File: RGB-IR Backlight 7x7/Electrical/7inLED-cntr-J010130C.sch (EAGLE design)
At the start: 52 parts, among them M1 TEENSY_3.1-3.2_DIL, P3 CON2X3, U1 LP2985-33DBVR, U2 AD5624R-3, U24 IL 710, U3 OPA4197IDR, U4 OPA4197IDR, U5 LMV344, U6 LMV344, U8 741G3157DBVR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

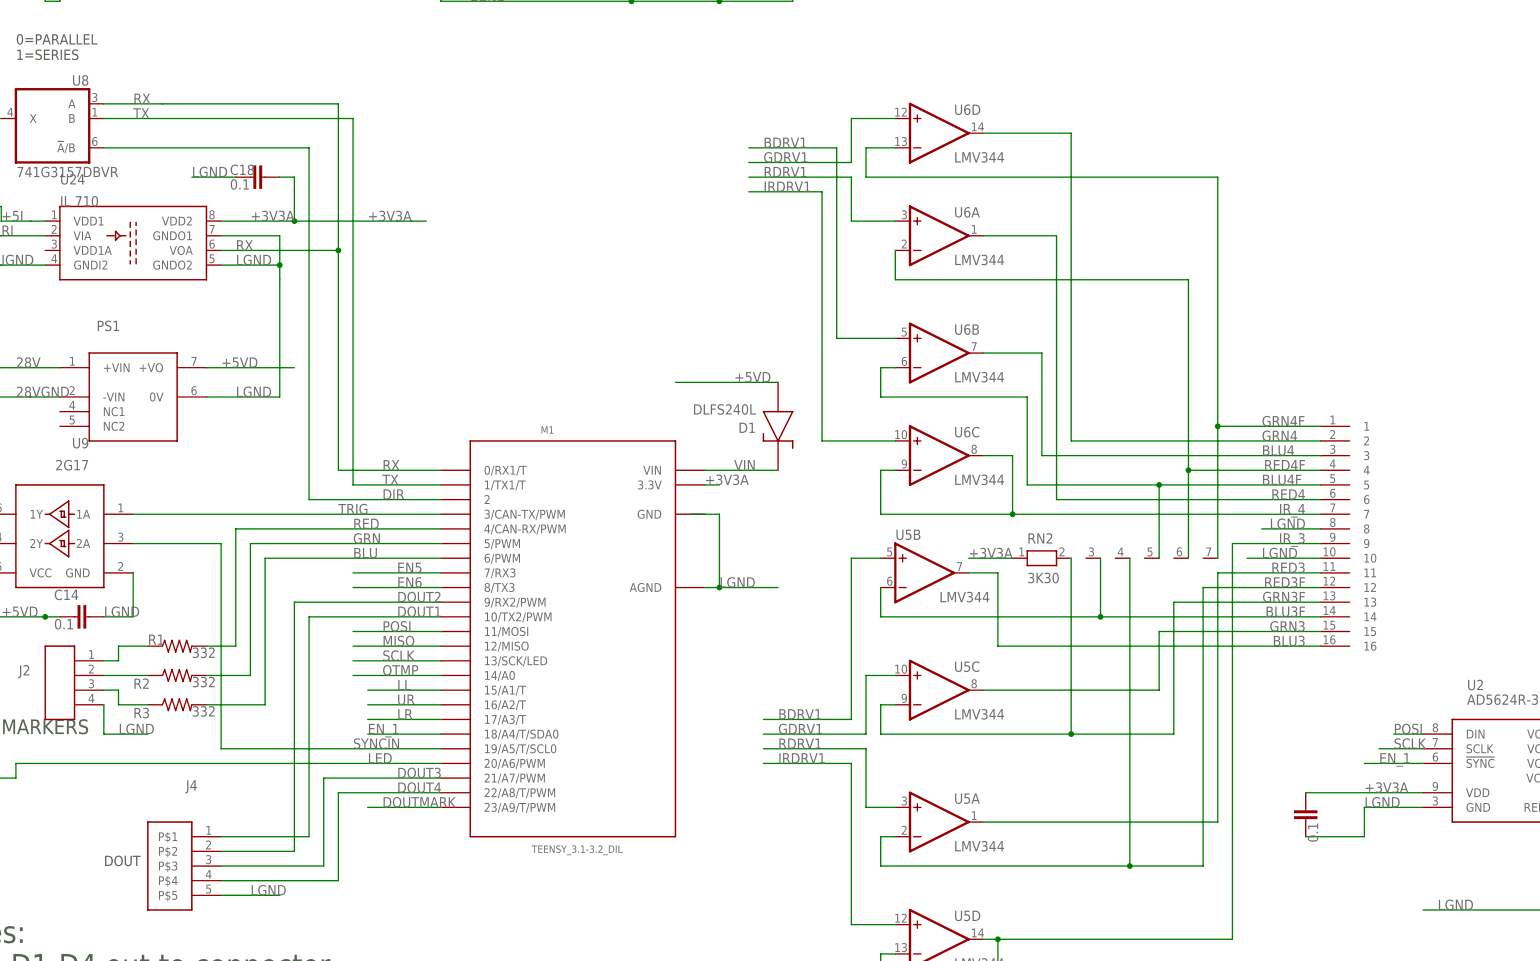
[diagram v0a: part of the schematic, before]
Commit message: board change and FW update
Change Teensy connector to two parts so it can be put into Circuithub
Fix markerCmd - digital changes weren't changing pin state
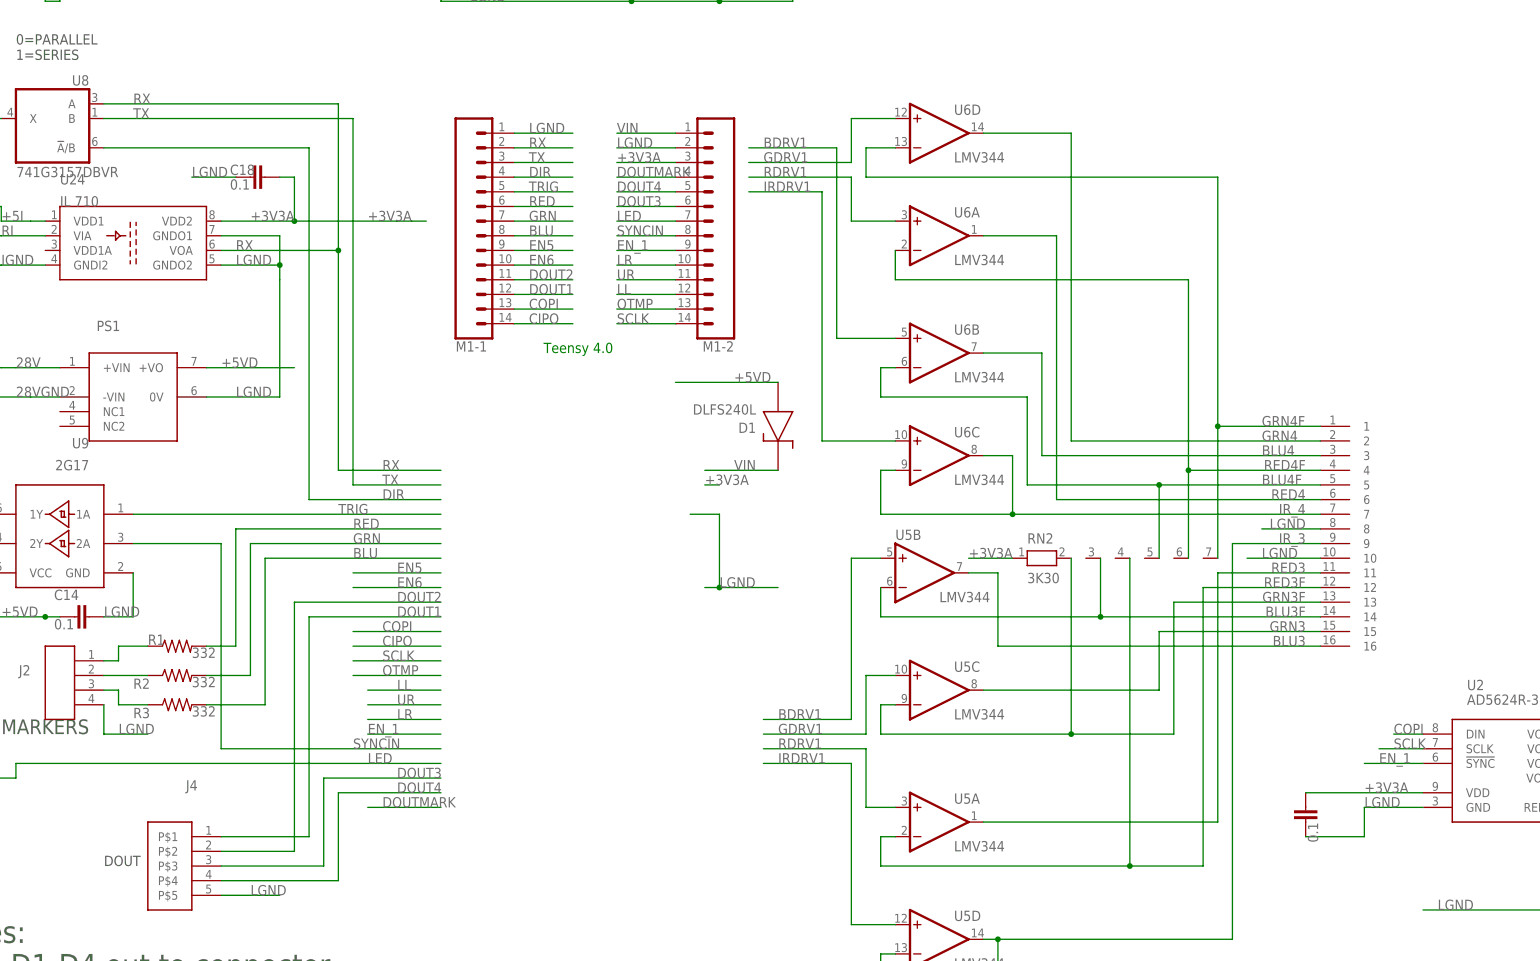
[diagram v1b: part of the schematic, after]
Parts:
- removed M1: TEENSY_3.1-3.2_DIL, Teensy_3_and_LC_Series_Boards_v1.4:TEENSY_3.1-3.2_DIL
- added M1-1, M1-2: (no value), SparkFun-Connectors:CONN_14
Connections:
- removed net MISO: M1.12/MISO
- removed net POSI: M1.11/MOSI, U2.DIN
- new net CIPO: M1-1.14
- new net COPI: M1-1.13, U2.DIN
- net +3V3A: now also M1-2.3; no longer M1.3.3V
- net BLU: now also M1-1.8; no longer M1.6/PWM
- net DIR: now also M1-1.4; no longer M1.2
- net DOUT1: now also M1-1.12; no longer M1.10/TX2/PWM
- net DOUT2: now also M1-1.11; no longer M1.9/RX2/PWM
- net DOUT3: now also M1-2.6; no longer M1.21/A7/PWM
- net DOUT4: now also M1-2.5; no longer M1.22/A8/T/PWM
- net DOUTMARK: now also M1-2.4; no longer M1.23/A9/T/PWM
- net EN5: now also M1-1.9; no longer M1.7/RX3
- net EN6: now also M1-1.10; no longer M1.8/TX3
- net EN_1: now also M1-2.9; no longer M1.18/A4/T/SDA0
- net GRN: now also M1-1.7; no longer M1.5/PWM
- net LED: now also M1-2.7; no longer M1.20/A6/PWM
- net LGND: now also M1-1.1, M1-2.2; no longer M1.AGND, M1.GND
- net LL: now also M1-2.12; no longer M1.15/A1/T
- net LR: now also M1-2.10; no longer M1.17/A3/T
- net OTMP: now also M1-2.13; no longer M1.14/A0
- net RED: now also M1-1.6; no longer M1.4/CAN-RX/PWM
- net RX: now also M1-1.2; no longer M1.0/RX1/T
- net SCLK: now also M1-2.14; no longer M1.13/SCK/LED
- net SYNCIN: now also M1-2.8; no longer M1.19/A5/T/SCL0
- net TRIG: now also M1-1.5; no longer M1.3/CAN-TX/PWM
- net TX: now also M1-1.3; no longer M1.1/TX1/T
- net UR: now also M1-2.11; no longer M1.16/A2/T
- net VIN: now also M1-2.1; no longer M1.VIN
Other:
- note added: "Teensy 4.0"

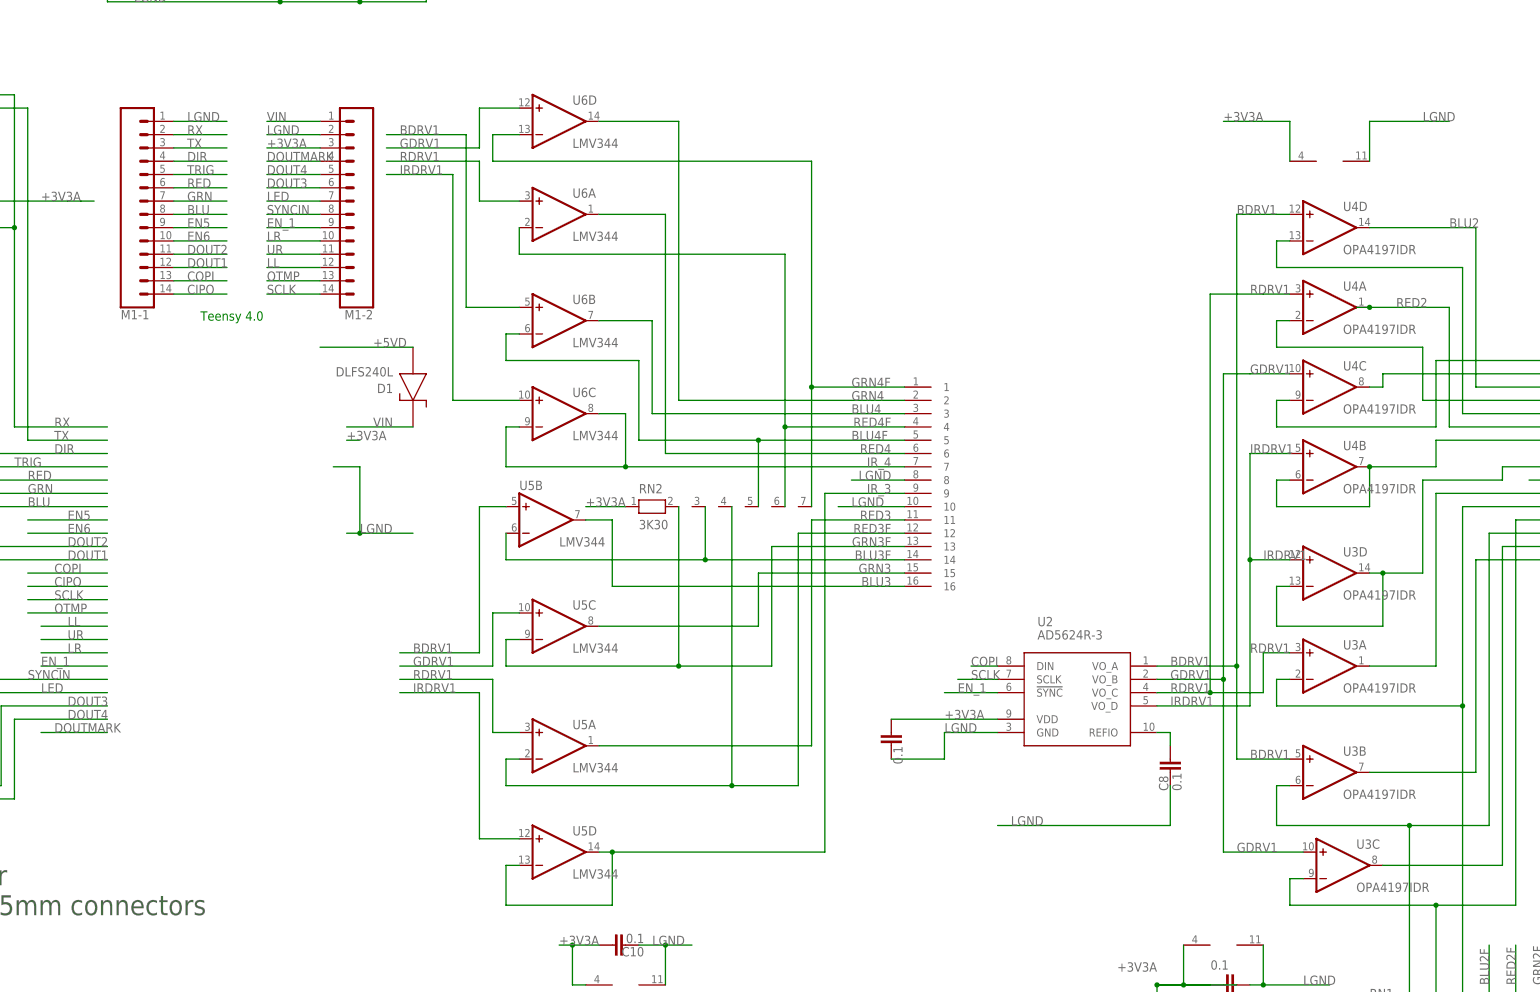
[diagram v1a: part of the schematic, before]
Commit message: Update BOM and firmware
Comment out DEBUG define in FW
Update costing in BOM
Correct quantities, etc in BOM
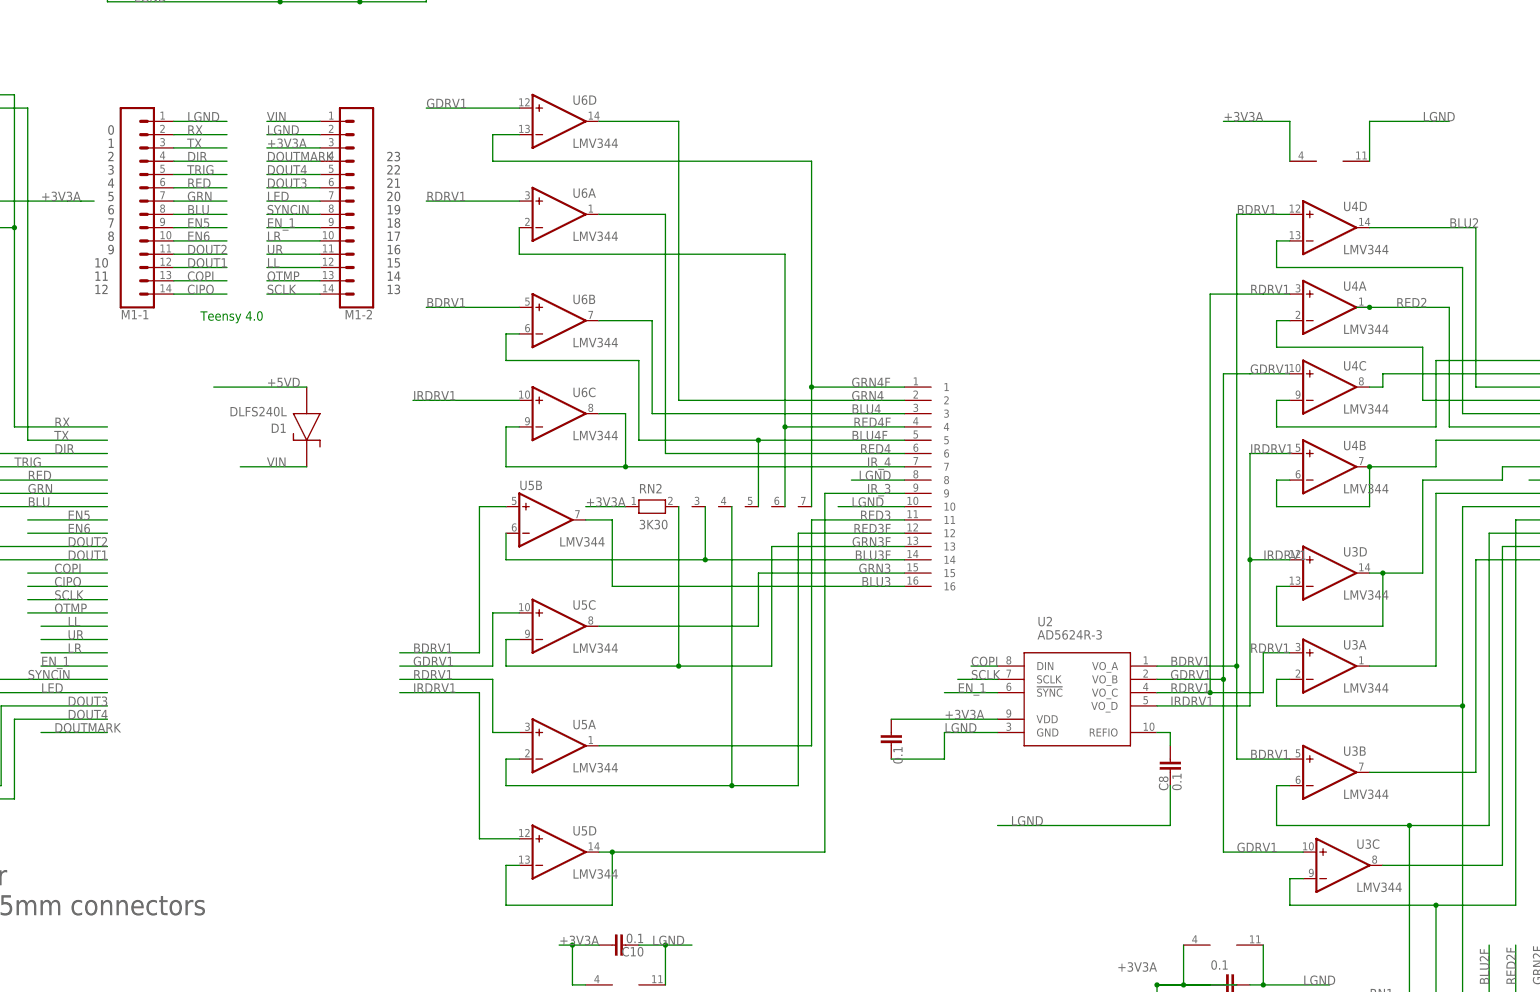
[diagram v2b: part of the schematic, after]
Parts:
- U3, U4: value OPA4197IDR -> LMV344
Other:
- note added: "0"
- note added: "1"
- note added: "10"
- note added: "11"
- note added: "12"
- note added: "13"
- note added: "14"
- note added: "15"
- note added: "16"
- note added: "17"
- note added: "18"
- note added: "19"
- note added: "2"
- note added: "20"
- note added: "21"
- note added: "22"
- note added: "23"
- note added: "3"
- note added: "4"
- note added: "5"
- note added: "6"
- note added: "7"
- note added: "8"
- note added: "9"
- moved on the sheet: D1
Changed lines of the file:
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@@
 <part name="C8" library="STEVES_BU" deviceset="CAPS" device="0603S" value="0.1"/>
 <part name="P1" library="STEVES_BU" deviceset="CON16" device="2X8PLUG"/>
-<part name="U4" library="adafruit" deviceset="QUAD_OPAMP" device="D" value="OPA4197IDR"/>
-<part name="U3" library="adafruit" deviceset="QUAD_OPAMP" device="D" value="OPA4197IDR"/>
+<part name="U4" library="adafruit" deviceset="QUAD_OPAMP" device="D" value="LMV344"/>
+<part name="U3" library="adafruit" deviceset="QUAD_OPAMP" device="D" value="LMV344"/>
 <part name="U5" library="adafruit" deviceset="QUAD_OPAMP" device="D" value="LMV344"/>
 <part name="U6" library="adafruit" deviceset="QUAD_OPAMP" device="D" value="LMV344"/>
@@
 <text x="281.94" y="177.8" size="1.778" layer="97">DOUT</text>
 <text x="358.14" y="266.7" size="1.778" layer="91">Teensy 4.0</text>
+<text x="340.36" y="302.26" size="1.778" layer="97">0</text>
+<text x="340.36" y="299.72" size="1.778" layer="97">1</text>
+<text x="340.36" y="297.18" size="1.778" layer="97">2</text>
+<text x="340.36" y="294.64" size="1.778" layer="97">3</text>
+<text x="340.36" y="292.1" size="1.778" layer="97">4</text>
+<text x="340.36" y="289.56" size="1.778" layer="97">5</text>
+<text x="340.36" y="287.02" size="1.778" layer="97">6</text>
+<text x="340.36" y="284.48" size="1.778" layer="97">7</text>
+<text x="340.36" y="281.94" size="1.778" layer="97">8</text>
+<text x="340.36" y="279.4" size="1.778" layer="97">9</text>
+<text x="337.82" y="276.86" size="1.778" layer="97">10</text>
+<text x="337.82" y="274.32" size="1.778" layer="97">11</text>
+<text x="337.82" y="271.78" size="1.778" layer="97">12</text>
+<text x="393.7" y="271.78" size="1.778" layer="97">13</text>
+<text x="393.7" y="274.32" size="1.778" layer="97">14</text>
+<text x="393.7" y="276.86" size="1.778" layer="97">15</text>
+<text x="393.7" y="279.4" size="1.778" layer="97">16</text>
+<text x="393.7" y="281.94" size="1.778" layer="97">17</text>
+<text x="393.7" y="284.48" size="1.778" layer="97">18</text>
+<text x="393.7" y="287.02" size="1.778" layer="97">19</text>
+<text x="393.7" y="289.56" size="1.778" layer="97">20</text>
+<text x="393.7" y="292.1" size="1.778" layer="97">21</text>
+<text x="393.7" y="294.64" size="1.778" layer="97">22</text>
+<text x="393.7" y="297.18" size="1.778" layer="97">23</text>
 </plain>
 <instances>
@@
 <attribute name="VALUE" x="303.784" y="295.021" size="1.778" layer="96"/>
 </instance>
-<instance part="D1" gate="G$1" x="398.78" y="254" smashed="yes" rot="R270">
-<attribute name="NAME" x="394.97" y="254.635" size="1.778" layer="95" rot="R180"/>
-<attribute name="VALUE" x="394.97" y="257.81" size="1.778" layer="96" rot="R180"/>
+<instance part="D1" gate="G$1" x="378.46" y="246.38" smashed="yes" rot="R270">
+<attribute name="NAME" x="374.65" y="247.015" size="1.778" layer="95" rot="R180"/>
+<attribute name="VALUE" x="374.65" y="250.19" size="1.778" layer="96" rot="R180"/>
 </instance>
 <instance part="J3" gate="G$1" x="228.6" y="238.76" rot="MR0"/>
@@
 <wire x1="492.76" y1="236.22" x2="482.6" y2="236.22" width="0.1524" layer="91"/>
 <label x="490.22" y="236.22" size="1.778" layer="95" rot="MR0"/>
-</segment>
-<segment>
-<wire x1="383.54" y1="238.76" x2="388.62" y2="238.76" width="0.1524" layer="91"/>
-<wire x1="388.62" y1="238.76" x2="388.62" y2="226.06" width="0.1524" layer="91"/>
-<wire x1="388.62" y1="226.06" x2="386.08" y2="226.06" width="0.1524" layer="91"/>
-<label x="388.62" y="226.06" size="1.778" layer="95"/>
-<wire x1="388.62" y1="226.06" x2="398.78" y2="226.06" width="0.1524" layer="91"/>
-<junction x="388.62" y="226.06"/>
 </segment>
 <segment>
@@
 <segment>
 <pinref part="D1" gate="G$1" pin="A"/>
-<wire x1="398.78" y1="261.62" x2="381" y2="261.62" width="0.1524" layer="91"/>
-<label x="391.16" y="261.62" size="1.778" layer="95"/>
+<wire x1="378.46" y1="254" x2="360.68" y2="254" width="0.1524" layer="91"/>
+<label x="370.84" y="254" size="1.778" layer="95"/>
 </segment>
 <segment>
@@
 </segment>
 <segment>
-<label x="396.24" y="302.26" size="1.778" layer="95"/>
+<label x="401.32" y="269.24" size="1.778" layer="95"/>
 <pinref part="U6" gate="B" pin="+IN"/>
-<wire x1="419.1" y1="269.24" x2="408.94" y2="269.24" width="0.1524" layer="91"/>
-<wire x1="408.94" y1="269.24" x2="408.94" y2="302.26" width="0.1524" layer="91"/>
-<wire x1="408.94" y1="302.26" x2="393.7" y2="302.26" width="0.1524" layer="91"/>
+<wire x1="419.1" y1="269.24" x2="401.32" y2="269.24" width="0.1524" layer="91"/>
 </segment>
 <segment>
@@
 </segment>
 <segment>
-<label x="396.24" y="299.72" size="1.778" layer="95"/>
-<wire x1="393.7" y1="299.72" x2="411.48" y2="299.72" width="0.1524" layer="91"/>
-<wire x1="411.48" y1="299.72" x2="411.48" y2="307.34" width="0.1524" layer="91"/>
-<wire x1="411.48" y1="307.34" x2="419.1" y2="307.34" width="0.1524" layer="91"/>
+<label x="401.32" y="307.34" size="1.778" layer="95"/>
+<wire x1="401.32" y1="307.34" x2="419.1" y2="307.34" width="0.1524" layer="91"/>
 <pinref part="U6" gate="D" pin="+IN"/>
 </segment>
@@
 </segment>
 <segment>
-<label x="396.24" y="297.18" size="1.778" layer="95"/>
+<label x="401.32" y="289.56" size="1.778" layer="95"/>
 <pinref part="U6" gate="A" pin="+IN"/>
-<wire x1="419.1" y1="289.56" x2="411.48" y2="289.56" width="0.1524" layer="91"/>
-<wire x1="411.48" y1="289.56" x2="411.48" y2="297.18" width="0.1524" layer="91"/>
-<wire x1="411.48" y1="297.18" x2="393.7" y2="297.18" width="0.1524" layer="91"/>
+<wire x1="419.1" y1="289.56" x2="401.32" y2="289.56" width="0.1524" layer="91"/>
 </segment>
 <segment>
@@
 </segment>
 <segment>
-<label x="396.24" y="294.64" size="1.778" layer="95"/>
+<label x="398.78" y="251.46" size="1.778" layer="95"/>
 <pinref part="U6" gate="C" pin="+IN"/>
-<wire x1="419.1" y1="251.46" x2="406.4" y2="251.46" width="0.1524" layer="91"/>
-<wire x1="406.4" y1="251.46" x2="406.4" y2="294.64" width="0.1524" layer="91"/>
-<wire x1="406.4" y1="294.64" x2="393.7" y2="294.64" width="0.1524" layer="91"/>
+<wire x1="419.1" y1="251.46" x2="398.78" y2="251.46" width="0.1524" layer="91"/>
 </segment>
 <segment>
@@
 <junction x="314.96" y="289.56"/>
 <wire x1="335.28" y1="289.56" x2="332.74" y2="289.56" width="0.1524" layer="91"/>
-</segment>
-<segment>
-<wire x1="386.08" y1="243.84" x2="388.62" y2="243.84" width="0.1524" layer="91"/>
-<label x="386.08" y="243.84" size="1.778" layer="95"/>
 </segment>
 <segment>
@@
 <net name="VIN" class="0">
 <segment>
-<wire x1="386.08" y1="246.38" x2="398.78" y2="246.38" width="0.1524" layer="91"/>
-<label x="391.16" y="246.38" size="1.778" layer="95"/>
+<wire x1="365.76" y1="238.76" x2="378.46" y2="238.76" width="0.1524" layer="91"/>
+<label x="370.84" y="238.76" size="1.778" layer="95"/>
 <pinref part="D1" gate="G$1" pin="K"/>
 </segment>
